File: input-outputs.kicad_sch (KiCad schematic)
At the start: 6 parts, among them J5 I2C-STEMMA-QT, J7 swd, J9 UART

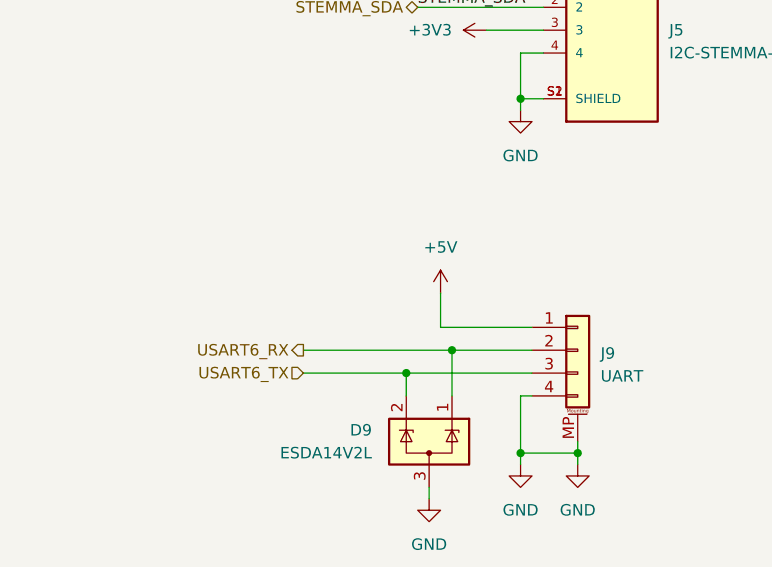
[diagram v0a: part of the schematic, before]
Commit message: Removing Camera, create alternative footprint for SPI LCD conn
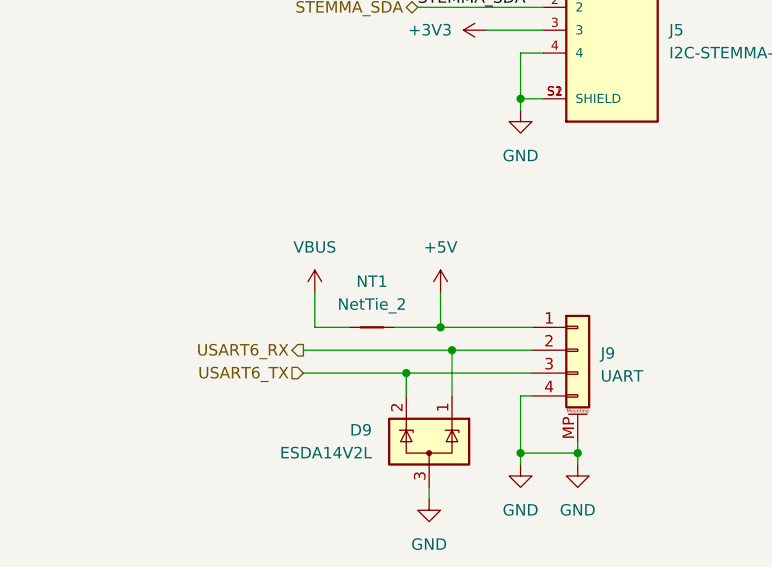
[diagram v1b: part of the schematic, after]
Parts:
- added NT1: NetTie_2, NetTie:NetTie-2_SMD_Pad0.5mm, symbol Device:NetTie_2
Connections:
- net +5V: now also NT1.2
- new net VBUS: NT1.1
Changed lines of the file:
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@@
+	)
+	(junction
+		(at 74.93 72.39)
+		(diameter 0)
+		(color 0 0 0 0)
 	)
 	(junction
@@
 	(wire
 		(pts
+			(xy 60.96 68.58) (xy 60.96 72.39)
+		)
+		(stroke
+			(width 0)
+			(type default)
+		)
+	)
+	(wire
+		(pts
+			(xy 69.85 72.39) (xy 74.93 72.39)
+		)
+		(stroke
+			(width 0)
+			(type default)
+		)
+	)
+	(wire
+		(pts
 			(xy 59.69 74.93) (xy 76.2 74.93)
 		)
@@
 		(pts
 			(xy 83.82 41.91) (xy 83.82 46.99)
+		)
+		(stroke
+			(width 0)
+			(type default)
+		)
+	)
+	(wire
+		(pts
+			(xy 60.96 72.39) (xy 64.77 72.39)
 		)
 		(stroke
@@
 	)
 	(symbol
+		(lib_id "Device:NetTie_2")
+		(at 67.31 72.39 0)
+		(unit 1)
+		(exclude_from_sim no)
+		(in_bom no)
+		(on_board yes)
+		(dnp no)
+		(fields_autoplaced yes)
+		(property "Reference" "NT1"
+			(at 67.31 67.31 0)
+			(effects
+				(font
+					(size 1.27 1.27)
+				)
+			)
+		)
+		(property "Value" "NetTie_2"
+			(at 67.31 69.85 0)
+			(effects
+				(font
+					(size 1.27 1.27)
+				)
+			)
+		)
+		(property "Footprint" "NetTie:NetTie-2_SMD_Pad0.5mm"
+			(at 67.31 72.39 0)
+			(effects
+				(font
+					(size 1.27 1.27)
+				)
+				(hide yes)
+			)
+		)
+		(property "Datasheet" "~"
+			(at 67.31 72.39 0)
+			(effects
+				(font
+					(size 1.27 1.27)
+				)
+				(hide yes)
+			)
+		)
+		(property "Description" "Net tie, 2 pins"
+			(at 67.31 72.39 0)
+			(effects
+				(font
+					(size 1.27 1.27)
+				)
+				(hide yes)
+			)
+		)
+		(pin "2"
+		)
+		(pin "1"
+		)
+		(instances
+			(project "chroma-pixel-zeta"
+				(path "/70094798-b7e4-48a4-a512-b8f48be18f9f/cf3c6c38-1b0f-4722-9440-d8d8f6f0e2e1"
+					(reference "NT1")
+					(unit 1)
+				)
+			)
+		)
+	)
+	(symbol
 		(lib_name "GND_1")
 		(lib_id "power:GND")
@@
 					(unit 1)
 				)
+			)
+		)
+	)
+	(symbol
+		(lib_id "power:VBUS")
+		(at 60.96 68.58 0)
+		(unit 1)
+		(exclude_from_sim no)
+		(in_bom yes)
+		(on_board yes)
+		(dnp no)
+		(fields_autoplaced yes)
+		(property "Reference" "#PWR0153"
+			(at 60.96 72.39 0)
+			(effects
+				(font
+					(size 1.27 1.27)
+				)
+				(hide yes)
+			)
+		)
+		(property "Value" "VBUS"
+			(at 60.96 63.5 0)
+			(effects
+				(font
+					(size 1.27 1.27)
+				)
+			)
+		)
+		(property "Footprint" ""
+			(at 60.96 68.58 0)
+			(effects
+				(font
+					(size 1.27 1.27)
+				)
+				(hide yes)
+			)
+		)
+		(property "Datasheet" ""
+			(at 60.96 68.58 0)
+			(effects
+				(font
+					(size 1.27 1.27)
+				)
+				(hide yes)
+			)
+		)
+		(property "Description" "Power symbol creates a global label with name \"VBUS\""
+			(at 60.96 68.58 0)
+			(effects
+				(font
+					(size 1.27 1.27)
+				)
+				(hide yes)
+			)
+		)
+		(pin "1"
+		)
+		(instances
+			(project "chroma-pixel-zeta"
+				(path "/70094798-b7e4-48a4-a512-b8f48be18f9f/cf3c6c38-1b0f-4722-9440-d8d8f6f0e2e1"
+					(reference "#PWR0153")
+					(unit 1)
+				)
